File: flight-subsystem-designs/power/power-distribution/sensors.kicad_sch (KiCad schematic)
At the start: 14 parts, among them U1 TMP36FSZ, U2 INA219AxD, U3 INA219AxD, U4 INA219AxD, U5 INA219AxD

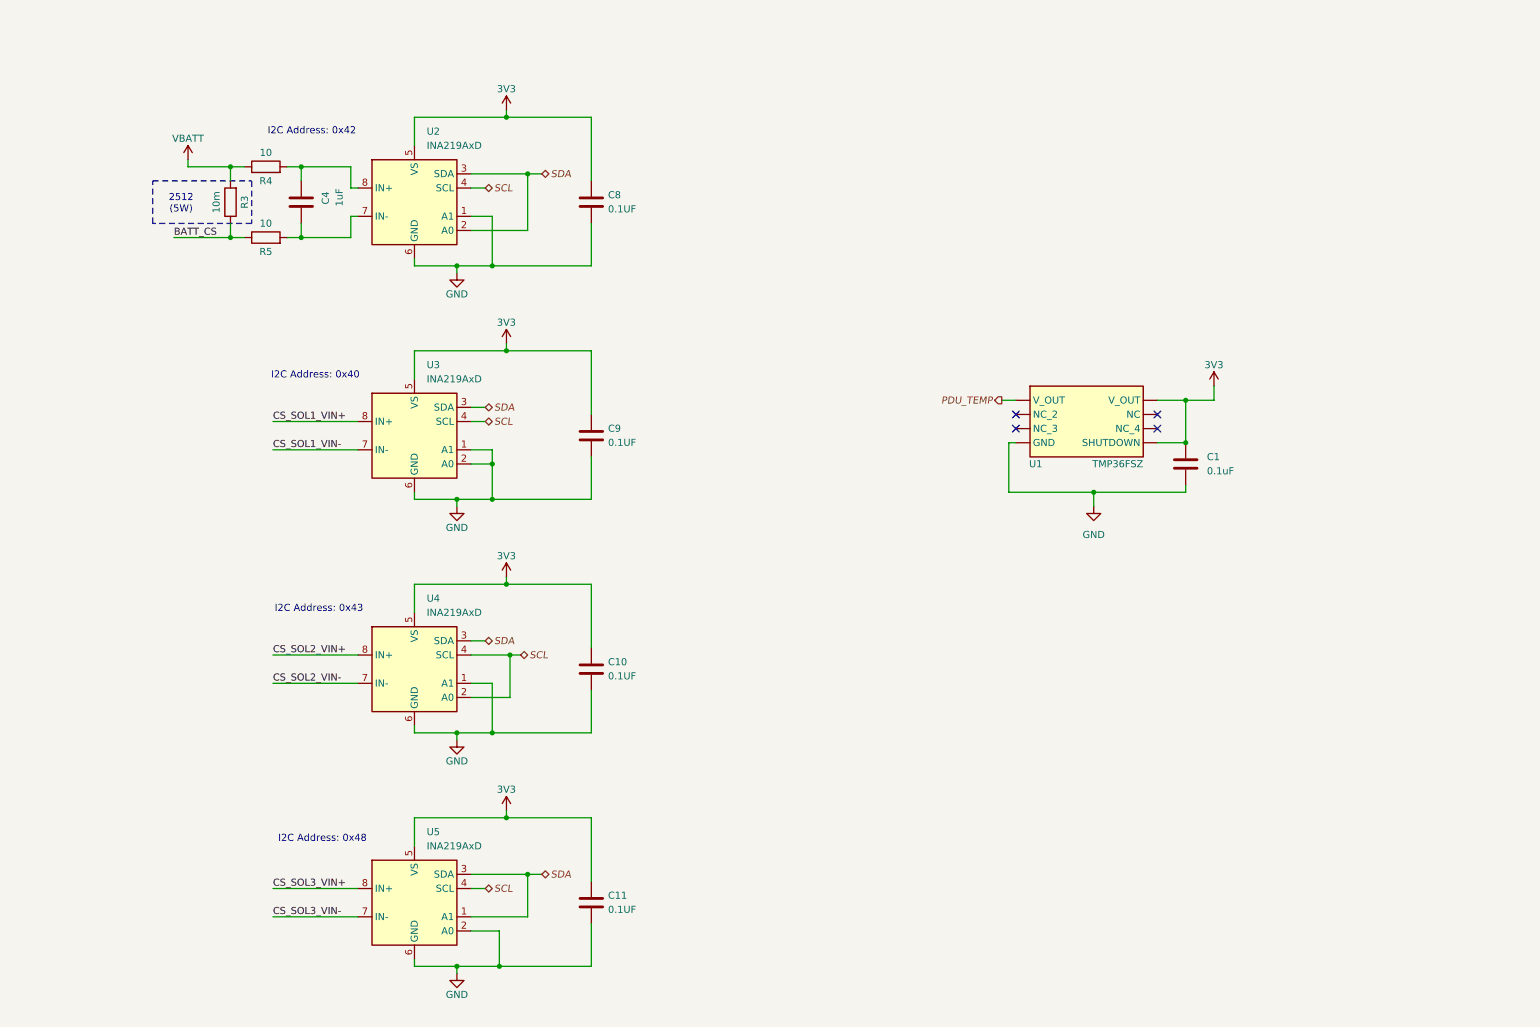
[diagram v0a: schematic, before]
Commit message: feat: PDU 4.0.0 (WIP)
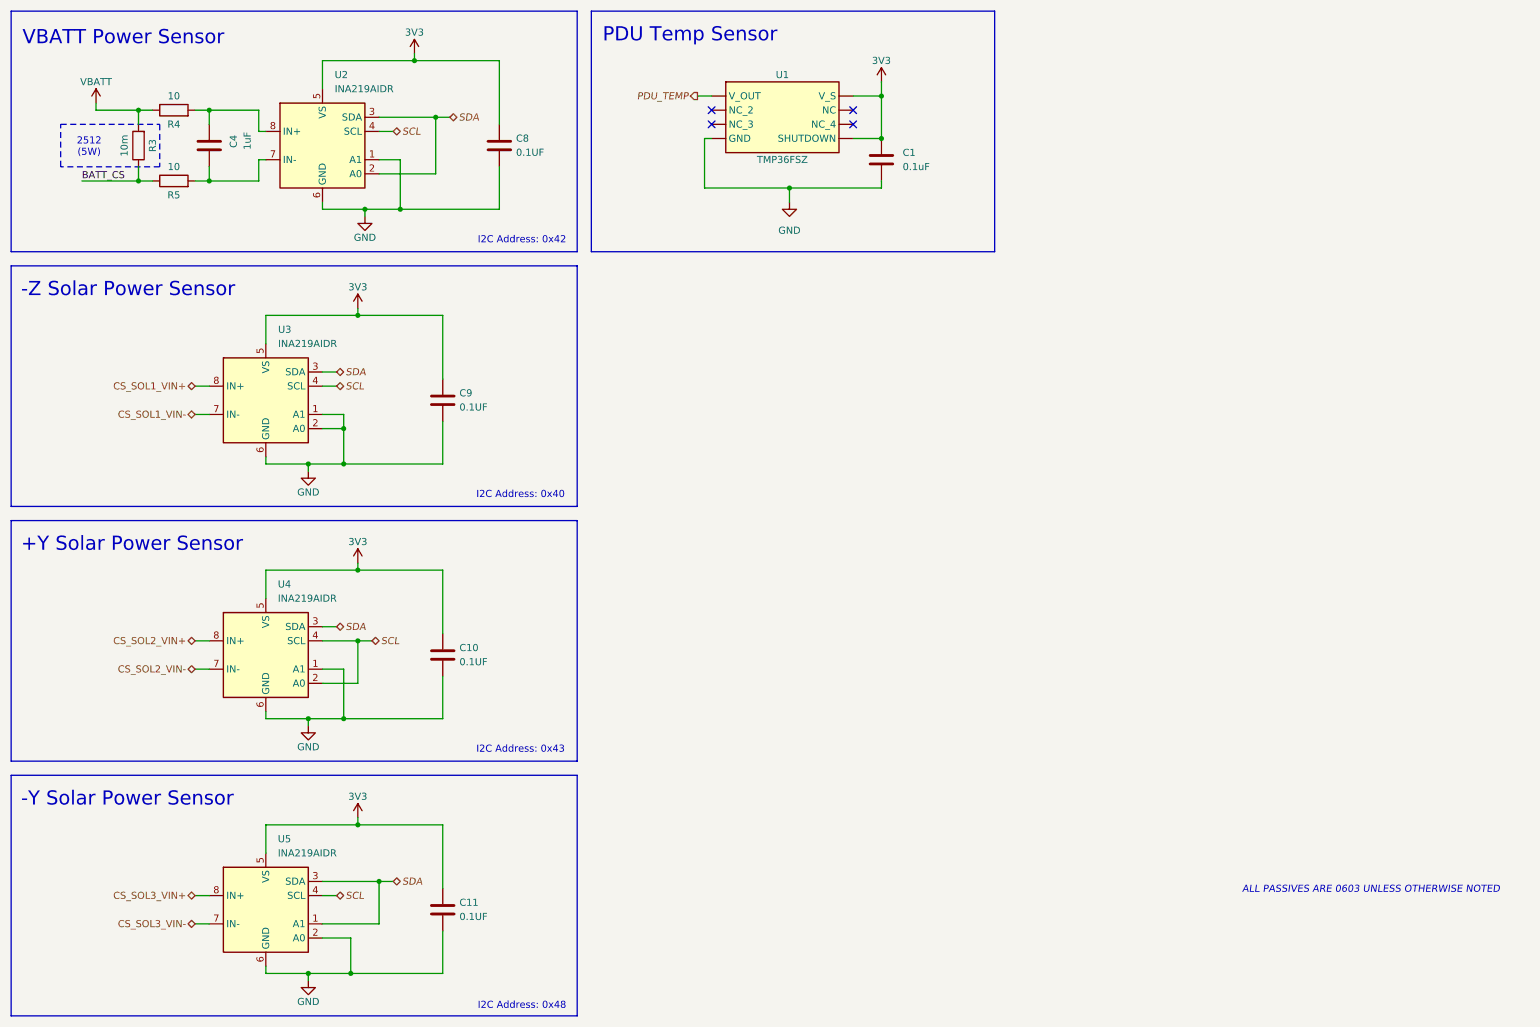
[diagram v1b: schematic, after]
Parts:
- U2, U3, U4, U5: value INA219AxD -> INA219AIDR
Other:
- note added: "+Y Solar Power Sensor"
- note added: "-Y Solar Power Sensor"
- note added: "-Z Solar Power Sensor"
- note added: "ALL PASSIVES ARE 0603 UNLESS OTHERWISE NOTED"
- note added: "PDU Temp Sensor"
- note added: "VBATT Power Sensor"
- moved on the sheet: C1, C10, C11, C4, C8, C9, R3, R4, R5, U1, U2, U3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

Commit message: shi
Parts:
- C10, C11, C8, C9: value 0.1UF -> 0.1uF
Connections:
- net 3V3: no longer C1.2, U1. (SHUTDOWN)
- net GND: now also U1.4 (GND); no longer U1. (SHUTDOWN)
- net PDU_TEMP: now also U1.1 (V_OUT); no longer U1. (SHUTDOWN)
- new net LDO_3V3: C1.2, U1.5 (SHUTDOWN), U1.8 (V_S)
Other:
- moved on the sheet: C1, C10, C11, C4, C8, C9, R3, R4, R5, U2
